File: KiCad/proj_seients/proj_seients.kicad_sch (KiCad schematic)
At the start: 0 parts

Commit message: Afegit Regulador de tensió +  Sensor Cinturó + CAN
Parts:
- added C1: 680uF, symbol Device:C_Polarized_US
- added C2: 220uF, symbol Device:C_Polarized_US
- added C3, C4, C7: 10uF, symbol Device:C
- added C5, C6: 22pF, symbol Device:C
- added D1, D2: 1N5822, Diode_THT:D_DO-201AD_P15.24mm_Horizontal, symbol Diode:1N5822
- added J1: BATERIA 12V, symbol Connector:Screw_Terminal_01x02
- added J2: Hebilla comercial con sensor integrado, symbol Connector:Screw_Terminal_01x02
- added J3: Conexiones al Bus del Coche, symbol Connector:Screw_Terminal_01x02
- added L1: 33uH, symbol Device:L
- added R1, R2, R3, R5: 10k, symbol Device:R
- added U1: PIC24HJ128GP502, Package_SO:SOIC-28W_7.5x17.9mm_P1.27mm, symbol DSP_Microchip_DSPIC33:DSPIC33FJ64MC802-xSP
- added U2: LM2596S-5, Package_TO_SOT_SMD:TO-263-5_TabPin3, symbol Regulator_Switching:LM2596S-5
- added U3: LM1117DT-3.3, Package_TO_SOT_SMD:TO-252-3_TabPin2, symbol Regulator_Linear:LM1117DT-3.3
- added U4: TCAN1043xDxQ1, Package_SO:SOIC-14_3.9x8.7mm_P1.27mm, symbol Interface_CAN_LIN:TCAN1043xDxQ1
- added Y1: Crystal, symbol Device:Crystal
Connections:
- new net: J3.1 (Pin_1), U4.13 (CANH)
- new net: J3.2 (Pin_2), U4.12 (CANL)
- new net: C5.2, U1.9 (OSC1/CLKI/CN30/RA2), Y1.1
- new net: C6.2, U1.10 (OSC2/CLKO/CN29/PMA0/RA3), Y1.2
- new net: R5.1, U1.1 (~{MCLR})
- new net: R3.1, U4.14 (~{STB})
- new net: D2.1 (K), L1.1, U2.2 (OUT)
- new net: R2.1, U4.6 (EN)
- new net: C7.2, U1.20 (VCAP)
- new net: D1.2 (A), J1.2 (Pin_2)
- new net 12V: C1.1, D1.1 (K), U2.1 (VIN), U4.10 (VSUP)
- new net 3,3V: C4.2, R1.1, R2.2, R3.2, R5.2, U1.13 (VDD), U3.2 (VO), U4.5 (VIO)
- new net 5V: C2.1, C3.2, U2.4 (FB), U3.3 (VI), U4.3 (VCC)
- new net CAN_RX: U1.23 (PWM1H2/RP12/CN14/PMD0/RB12), U4.4 (RXD)
- new net CAN_TX: U1.22 (PGEC2/TMS/PWM1L3/RP11/CN15/PMD1/RB11), U4.1 (TXD)
- new net CINT: J2.2 (Pin_2), R1.2, U1.14 (PGED3/ASDA1/RP5/CN27/PMD7/RB5)
- new net GND: C1.2, C2.2, C3.1, C4.1, C5.1, C6.1, C7.1, D2.2 (A), J1.1 (Pin_1), J2.1 (Pin_1), L1.2, U1.19 (VSS), U1.8 (VSS), U2.3 (GND), U2.5 (~{ON}/OFF), U3.1 (GND), U4.2 (GND), U4.9 (WAKE)
- no-connect marks 0 -> 2
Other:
- note added: "CLOCK"
- note added: "Regulador de Tensió"

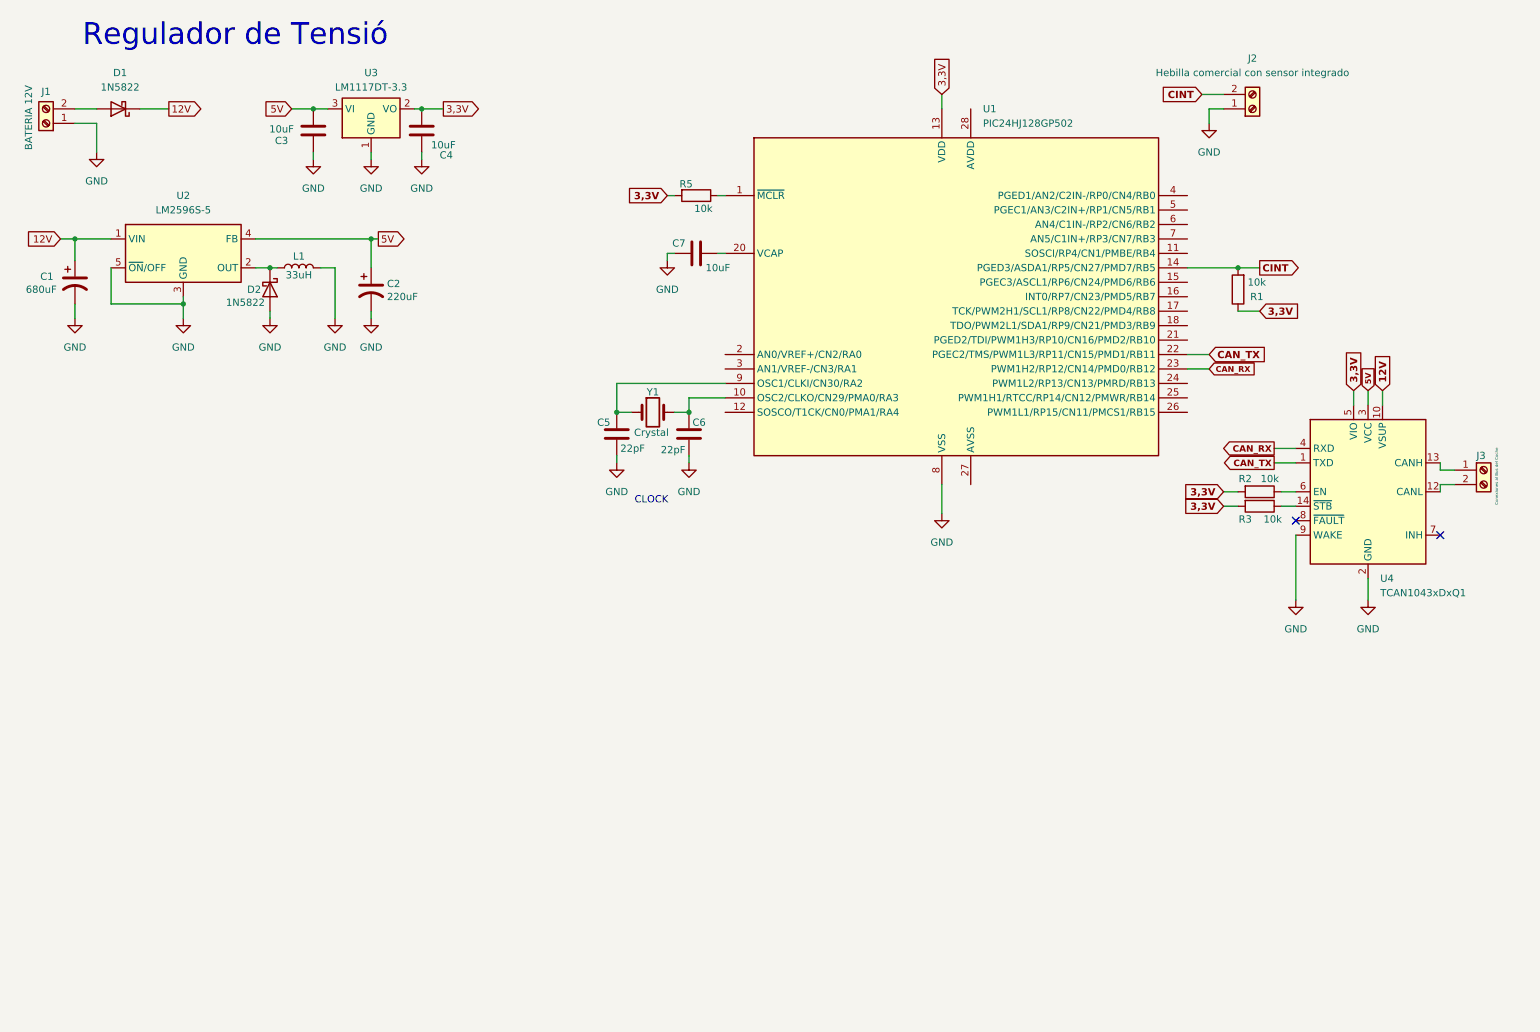
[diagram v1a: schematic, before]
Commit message: Afegit drivers + motors
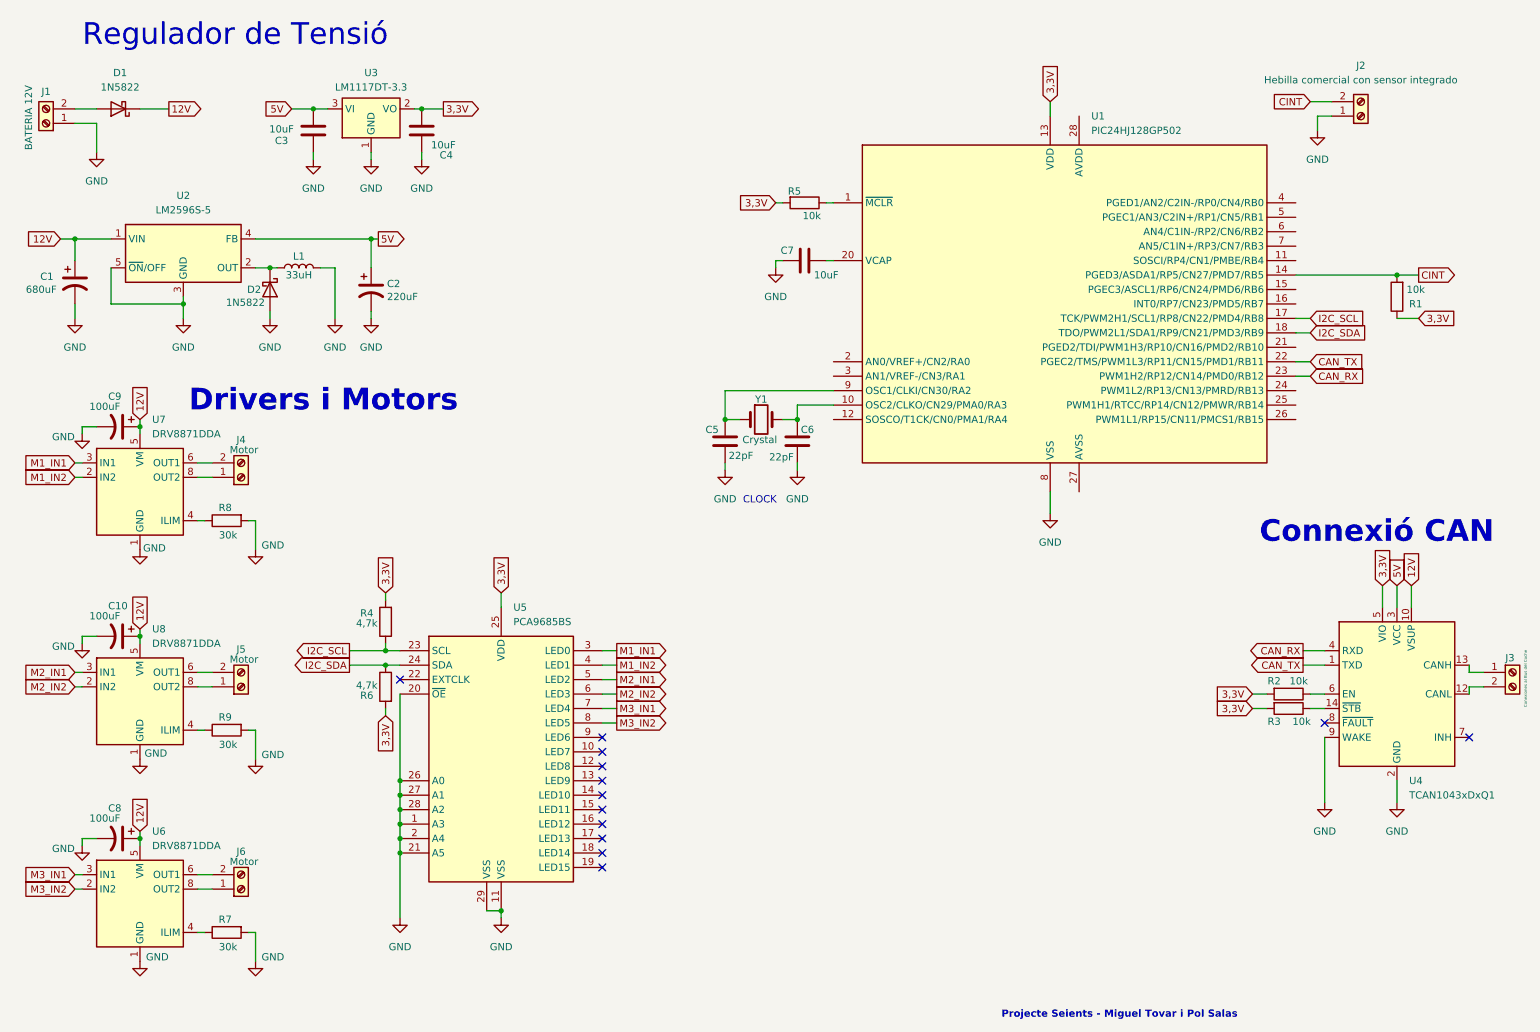
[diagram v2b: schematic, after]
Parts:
- added C10, C8, C9: 100uF, symbol Device:C_Polarized_US
- added J4, J5, J6: Motor, symbol Connector:Screw_Terminal_01x02
- added R4, R6: 4,7k, symbol Device:R
- added R7, R8, R9: 30k, symbol Device:R
- added U5: PCA9685BS, Package_DFN_QFN:QFN-28-1EP_6x6mm_P0.65mm_EP4.25x4.25mm, symbol Driver_LED:PCA9685BS
- added U6, U7, U8: DRV8871DDA, Package_SO:Texas_HTSOP-8-1EP_3.9x4.9mm_P1.27mm_EP2.95x4.9mm_Mask2.4x3.1mm_ThermalVias, symbol Driver_Motor:DRV8871DDA
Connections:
- net 12V: now also C10.1, C8.1, C9.1, U6.5 (VM), U7.5 (VM), U8.5 (VM)
- net 3,3V: now also R4.2, R6.2, U5.25 (VDD)
- net GND: now also C10.2, C8.2, C9.2, R7.2, R8.2, R9.2, U5.1 (A3), U5.11 (VSS), U5.2 (A4), U5.20 (~{OE}), U5.21 (A5), U5.26 (A0), U5.27 (A1), U5.28 (A2), U5.29 (VSS), U6.1 (GND), U6.7 (GND), U6.9 (GND), U7.1 (GND), U7.7 (GND), U7.9 (GND), U8.1 (GND), U8.7 (GND), U8.9 (GND)
- net I2C_SCL: now reaches U1.17 (TCK/PWM2H1/SCL1/RP8/CN22/PMD4/RB8)
- net I2C_SCL: now also R4.1, U5.23 (SCL)
- net I2C_SDA: now reaches U1.18 (TDO/PWM2L1/SDA1/RP9/CN21/PMD3/RB9)
- net I2C_SDA: now also R6.1, U5.24 (SDA)
- new net: R8.1, U7.4 (ILIM)
- new net: J4.2 (Pin_2), U7.6 (OUT1)
- new net: J4.1 (Pin_1), U7.8 (OUT2)
- new net: R9.1, U8.4 (ILIM)
- new net: J5.2 (Pin_2), U8.6 (OUT1)
- new net: J5.1 (Pin_1), U8.8 (OUT2)
- new net: J6.1 (Pin_1), U6.8 (OUT2)
- new net: J6.2 (Pin_2), U6.6 (OUT1)
- new net: R7.1, U6.4 (ILIM)
- new net M1_IN1: U5.3 (LED0), U7.3 (IN1)
- new net M1_IN2: U5.4 (LED1), U7.2 (IN2)
- new net M2_IN1: U5.5 (LED2), U8.3 (IN1)
- new net M2_IN2: U5.6 (LED3), U8.2 (IN2)
- new net M3_IN1: U5.7 (LED4), U6.3 (IN1)
- new net M3_IN2: U5.8 (LED5), U6.2 (IN2)
- no-connect marks 2 -> 13
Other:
- note added: "Connexió CAN"
- note added: "Drivers i Motors"
- note added: "Projecte Seients - Miguel Tovar i Pol Salas"
- moved on the sheet: C5, C6, C7, J2, J3, R1, R2, R3, R5, U1, U4, Y1
